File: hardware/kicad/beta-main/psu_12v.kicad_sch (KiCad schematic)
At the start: 0 parts

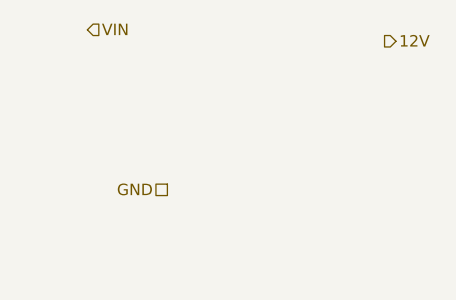
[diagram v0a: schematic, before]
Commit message: 5V and amplifier corrections
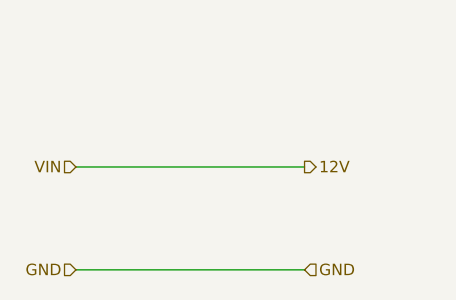
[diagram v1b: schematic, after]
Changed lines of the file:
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@@
 	(generator_version "9.0")
 	(paper "A4")
+	(title_block
+		(comment 1 "Powers: Servo Controller")
+	)
+	(wire
+		(pts
+			(xy 86.36 80.01) (xy 111.76 80.01)
+		)
+		(stroke
+			(width 0)
+			(type default)
+		)
+	)
+	(wire
+		(pts
+			(xy 86.36 91.44) (xy 111.76 91.44)
+		)
+		(stroke
+			(width 0)
+			(type default)
+		)
+	)
 	(hierarchical_label "12V"
 		(shape output)
-		(at 120.65 66.04 0)
+		(at 111.76 80.01 0)
 		(effects
 			(font
@@
 	)
 	(hierarchical_label "GND"
-		(shape passive)
-		(at 96.52 82.55 180)
+		(shape input)
+		(at 111.76 91.44 0)
+		(effects
+			(font
+				(size 1.27 1.27)
+			)
+			(justify left)
+		)
+	)
+	(hierarchical_label "VIN"
+		(shape input)
+		(at 86.36 80.01 180)
 		(effects
 			(font
@@
 		)
 	)
-	(hierarchical_label "VIN"
+	(hierarchical_label "GND"
 		(shape input)
-		(at 87.63 64.77 0)
+		(at 86.36 91.44 180)
 		(effects
 			(font
 				(size 1.27 1.27)
 			)
-			(justify left)
+			(justify right)
 		)
 	)
